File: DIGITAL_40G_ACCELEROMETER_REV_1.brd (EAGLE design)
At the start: 19 x 40.1 mm, 18 parts, among them IC1 ADIS16500AMLZ, IC2 LTC6820IUD#PBF, IC3 LDL1117S33R, T1 782482_33VC

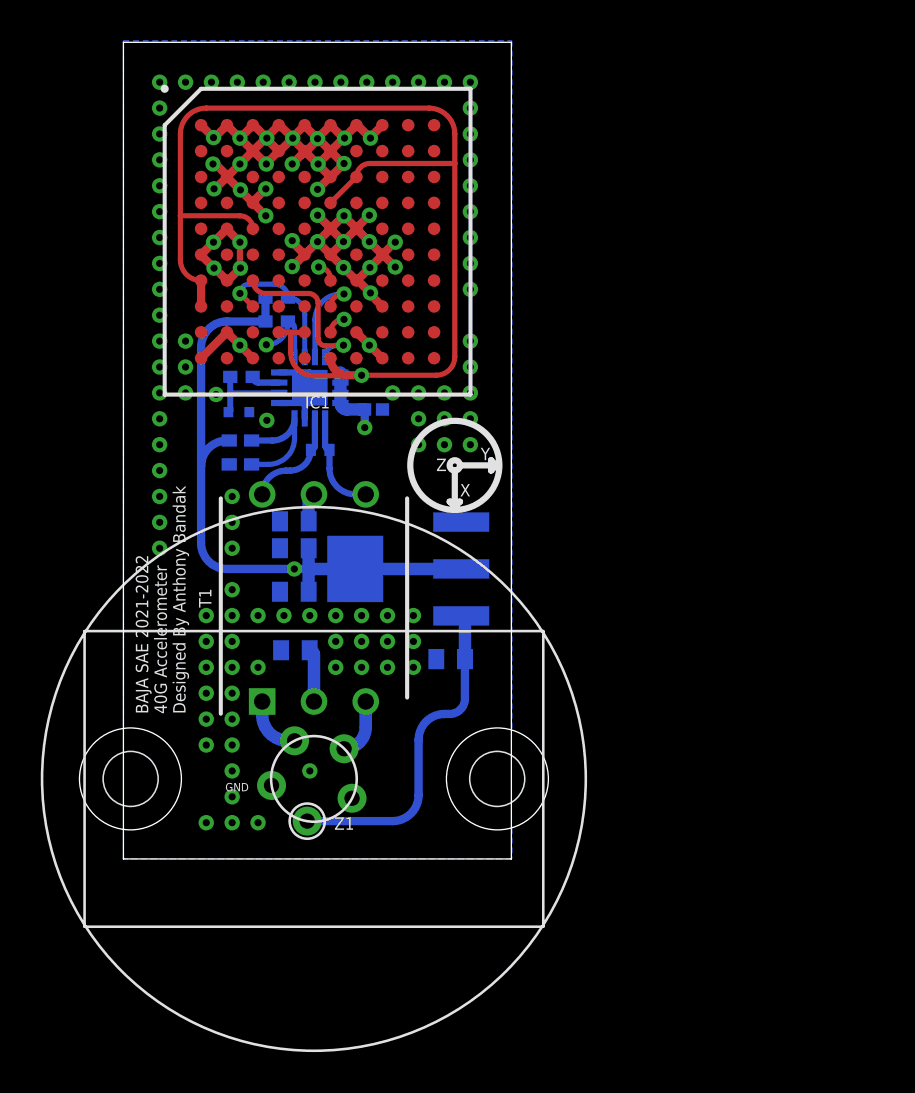
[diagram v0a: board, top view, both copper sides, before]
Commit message: Final Board Layout Update. Incorporated new connector model.
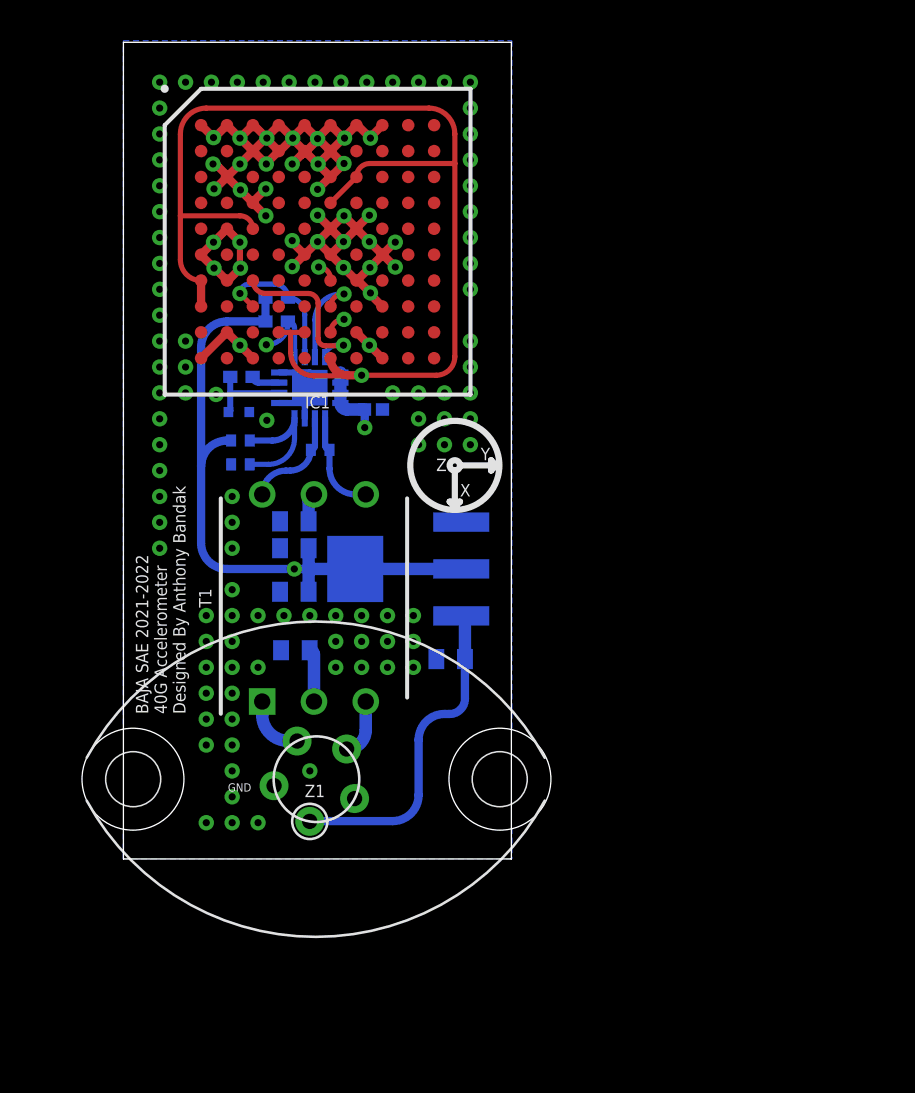
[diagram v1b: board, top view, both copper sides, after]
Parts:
- R11: device TNPW0402100RBYEP:RESC1005X40N -> SamacSys_Parts:RESC1005X40N
- R16, R17: device CRG0402ZR:RESC1005X40N -> SamacSys_Parts:RESC1005X40N
- moved Z1 13.3 mm to (9.40, 3.96)
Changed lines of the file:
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@@
 <drawing>
 <settings>
-<setting alwaysvectorfont="yes"/>
+<setting alwaysvectorfont="no"/>
 <setting verticaltext="up"/>
 </settings>
@@
 </layers>
 <board>
-<fusionsync huburn="a.YnVzaW5lc3M6bXljcHA1NTk" projecturn="a.YnVzaW5lc3M6bXljcHA1NTkjRDIwMjEwOTE1NDQ0OTgwODU2" f3durn="urn:adsk.wipprod:dm.lineage:BeAIdd1JT46-xdl6n52ekA" pcbguid="" lastpulledtime="" lastsyncedchangeguid="" latestrevisionid="1bc7ff69-2360-4ecd-9c21-a148a7abfcbe" lastsyncedrevisionid="1bc7ff69-2360-4ecd-9c21-a148a7abfcbe" lastboardhashguid="e5a5a45a-0394-a7ea-7430-f946065ce0ce" lastpushedtime="2022-03-26T00:00:16Z" linktopcb3d="true"/>
+<fusionsync huburn="a.YnVzaW5lc3M6bXljcHA1NTk" projecturn="a.YnVzaW5lc3M6bXljcHA1NTkjRDIwMjEwOTE1NDQ0OTgwODU2" f3durn="urn:adsk.wipprod:dm.lineage:BeAIdd1JT46-xdl6n52ekA" pcbguid="" lastpulledtime="" lastsyncedchangeguid="" latestrevisionid="42d7c380-4da1-460d-9f28-112faf3eeb5c" lastsyncedrevisionid="42d7c380-4da1-460d-9f28-112faf3eeb5c" lastboardhashguid="adb813b8-7e80-92ce-5e99-bf921410aa5f" lastpushedtime="2022-04-08T20:49:55Z" linktopcb3d="true"/>
 <plain>
 <wire x1="0" y1="0" x2="19.03" y2="0" width="0" layer="20"/>
@@
 <attribute name="NAME" x="13.97" y="18.288" size="0.6096" layer="26" rot="MR0" align="center"/>
 </element>
-<element name="R11" library="TNPW0402100RBYEP" package="RESC1005X40N" value="100" x="9.652" y="20.066" smashed="yes" rot="MR0">
+<element name="R11" library="SamacSys_Parts" library_urn="urn:adsk.eagle:library:34029941" package="RESC1005X40N" package3d_urn="urn:adsk.eagle:package:34740186/6" value="100" x="9.652" y="20.066" smashed="yes" rot="MR0">
 <attribute name="AVAILABILITY" value="In Stock" x="-22.098" y="-28.194" size="1.778" layer="28" rot="MR0" display="off"/>
 <attribute name="DESCRIPTION" value=" 100 Ohms ±0.1% 0.063W, 1/16W Chip Resistor 0402 (1005 Metric) Anti-Sulfur, Automotive AEC-Q200, Moisture Resistant Thin Film " x="-22.098" y="-28.194" size="1.778" layer="28" rot="MR0" display="off"/>
@@
 <attribute name="NAME" x="4.0132" y="12.8016" size="0.6096" layer="25" rot="R90" align="center"/>
 </element>
-<element name="Z1" library="SamacSys_Parts" library_urn="urn:adsk.eagle:library:31941355" package="AS_FEMALE_5_PIN" package3d_urn="urn:adsk.eagle:package:34263750/6" value="AS_FEMALE_5_PIN" x="20.574" y="11.176" smashed="yes" rot="R180">
-<attribute name="NAME" x="10.8372" y="1.7346" size="0.6096" layer="25" rot="R180" align="center"/>
-</element>
-<element name="R16" library="CRG0402ZR" package="RESC1005X40N" value="CRG0402ZR" x="5.7404" y="19.3548" smashed="yes" rot="MR0">
+<element name="Z1" library="SamacSys_Parts" library_urn="urn:adsk.eagle:library:31941355" package="AS_FEMALE_5_PIN" package3d_urn="urn:adsk.eagle:package:34263750/8" value="AS_FEMALE_5_PIN" x="9.398" y="3.9624" smashed="yes" rot="R180">
+<attribute name="NAME" x="9.3894" y="3.3348" size="0.6096" layer="25" rot="R180" align="center"/>
+</element>
+<element name="R16" library="SamacSys_Parts" library_urn="urn:adsk.eagle:library:34029941" package="RESC1005X40N" package3d_urn="urn:adsk.eagle:package:34740186/6" value="CRG0402ZR" x="5.7404" y="19.3548" smashed="yes" rot="MR0">
 <attribute name="DESCRIPTION" value="0 0402 Thick Film Surface Mount Fixed Resistor +/-0% 0.063W CRG0402ZR" x="5.7404" y="19.3548" size="1.778" layer="28" rot="MR0" display="off"/>
 <attribute name="HEIGHT" value="0.4mm" x="5.7404" y="19.3548" size="1.778" layer="28" rot="MR0" display="off"/>
@@
 <attribute name="NAME" x="3.5814" y="19.3548" size="0.6096" layer="26" rot="MR0" align="center"/>
 </element>
-<element name="R17" library="CRG0402ZR" package="RESC1005X40N" value="CRG0402ZR" x="5.7404" y="20.5232" smashed="yes" rot="MR0">
+<element name="R17" library="SamacSys_Parts" library_urn="urn:adsk.eagle:library:34029941" package="RESC1005X40N" package3d_urn="urn:adsk.eagle:package:34740186/6" value="CRG0402ZR" x="5.7404" y="20.5232" smashed="yes" rot="MR0">
 <attribute name="DESCRIPTION" value="0 0402 Thick Film Surface Mount Fixed Resistor +/-0% 0.063W CRG0402ZR" x="5.7404" y="20.5232" size="1.778" layer="28" rot="MR0" display="off"/>
 <attribute name="HEIGHT" value="0.4mm" x="5.7404" y="20.5232" size="1.778" layer="28" rot="MR0" display="off"/>
@@
 <wire x1="10.16" y1="25.8318" x2="10.795" y2="26.4668" width="0.254" layer="1" curve="-90"/>
 <wire x1="10.795" y1="26.4668" x2="10.8204" y2="26.4668" width="0.254" layer="1"/>
-<wire x1="11.215" y1="2.976" x2="12.446" y2="2.976" width="0.254" layer="2"/>
-<wire x1="12.446" y1="2.976" x2="13.716" y2="4.246" width="0.254" layer="2" curve="90"/>
+<wire x1="13.716" y1="4.246" x2="12.446" y2="2.976" width="0.254" layer="2" curve="-90"/>
 <wire x1="13.716" y1="6.604" x2="14.986" y2="7.874" width="0.254" layer="2" curve="-90"/>
 <wire x1="17.78" y1="9.144" x2="16.51" y2="7.874" width="0.254" layer="2" curve="-90"/>
@@
 <wire x1="16.51" y1="26.4668" x2="17.78" y2="25.1968" width="0.254" layer="2" curve="-90"/>
 <wire x1="17.78" y1="25.1968" x2="17.78" y2="9.144" width="0.254" layer="2"/>
+<wire x1="12.446" y1="2.976" x2="11.3526" y2="2.976" width="0.254" layer="2"/>
+<wire x1="11.3526" y1="2.976" x2="11.339" y2="2.9624" width="0.254" layer="2" curve="90"/>
 </signal>
 <signal name="IP">
 <contactref element="T1" pad="1"/>
 <contactref element="Z1" pad="5"/>
-<wire x1="8.395" y1="5.796" x2="8.0772" y2="5.796" width="0.6096" layer="16"/>
 <wire x1="8.0772" y1="5.796" x2="6.8072" y2="7.066" width="0.6096" layer="16" curve="-90"/>
 <wire x1="6.8072" y1="7.066" x2="6.8072" y2="7.7216" width="0.6096" layer="16"/>
+<wire x1="8.519" y1="5.7824" x2="8.0908" y2="5.7824" width="0.6096" layer="16"/>
+<wire x1="8.0908" y1="5.7824" x2="8.0772" y2="5.796" width="0.6096" layer="16" curve="-90"/>
 </signal>
 <signal name="IM">
 <contactref element="T1" pad="3"/>
 <contactref element="Z1" pad="4"/>
-<wire x1="10.825" y1="5.406" x2="11.8872" y2="6.4682" width="0.6096" layer="16" curve="90"/>
-<wire x1="11.8872" y1="6.4682" x2="11.8872" y2="7.7216" width="0.6096" layer="16"/>
+<wire x1="11.8872" y1="6.3306" x2="10.949" y2="5.3924" width="0.6096" layer="16" curve="-90"/>
+<wire x1="11.8872" y1="7.7216" x2="11.8872" y2="6.3306" width="0.6096" layer="16"/>
 </signal>
 <signal name="12V">
@@
 <wire x1="16.7528" y1="9.8044" x2="16.7528" y2="11.7412" width="0.6096" layer="16"/>
 <wire x1="16.7528" y1="11.7412" x2="16.57" y2="11.924" width="0.6096" layer="16" curve="90"/>
-<wire x1="9.015" y1="1.856" x2="13.208" y2="1.856" width="0.4064" layer="16"/>
-<wire x1="13.208" y1="1.856" x2="14.478" y2="3.126" width="0.4064" layer="16" curve="90"/>
+<wire x1="14.478" y1="3.126" x2="13.208" y2="1.856" width="0.4064" layer="16" curve="-90"/>
 <wire x1="14.478" y1="5.842" x2="15.748" y2="7.112" width="0.4064" layer="16" curve="-90"/>
 <wire x1="15.748" y1="7.112" x2="16.002" y2="7.112" width="0.4064" layer="16"/>
@@
 <wire x1="16.7528" y1="7.8628" x2="16.7528" y2="9.8044" width="0.4064" layer="16"/>
 <wire x1="14.478" y1="3.126" x2="14.478" y2="5.842" width="0.4064" layer="16"/>
+<wire x1="13.208" y1="1.856" x2="9.1526" y2="1.856" width="0.4064" layer="16"/>
+<wire x1="9.1526" y1="1.856" x2="9.139" y2="1.8424" width="0.4064" layer="16" curve="90"/>
 </signal>
 <signal name="3.3V">
@@
 <wire x1="11.8364" y1="22.039" x2="11.8282" y2="22.0472" width="0.4064" layer="16" curve="90"/>
 <wire x1="12.954" y1="15.494" x2="12.954" y2="20.0406" width="0.4064" layer="2"/>
-<wire x1="5.1904" y1="20.5232" x2="5.08" y2="20.5232" width="0.4064" layer="16"/>
+<wire x1="5.2834" y1="20.5232" x2="5.08" y2="20.5232" width="0.4064" layer="16"/>
 <wire x1="5.08" y1="20.5232" x2="3.81" y2="19.2532" width="0.4064" layer="16" curve="90"/>
 <wire x1="3.81" y1="15.494" x2="5.08" y2="14.224" width="0.4064" layer="16" curve="90"/>
@@
 <contactref element="R17" pad="1"/>
 <wire x1="8.394" y1="21.614" x2="7.3032" y2="20.5232" width="0.3048" layer="16" curve="-90"/>
-<wire x1="7.3032" y1="20.5232" x2="6.2904" y2="20.5232" width="0.3048" layer="16"/>
+<wire x1="7.3032" y1="20.5232" x2="6.1974" y2="20.5232" width="0.3048" layer="16"/>
 <wire x1="8.394" y1="21.614" x2="8.394" y2="20.6248" width="0.254" layer="16"/>
 <wire x1="8.394" y1="20.6248" x2="7.124" y2="19.3548" width="0.254" layer="16" curve="-90"/>
-<wire x1="7.124" y1="19.3548" x2="6.2904" y2="19.3548" width="0.254" layer="16"/>
+<wire x1="7.124" y1="19.3548" x2="6.1974" y2="19.3548" width="0.254" layer="16"/>
 </signal>
 <signal name="N$1">

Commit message: Final final board layout update. Screw mounted now.
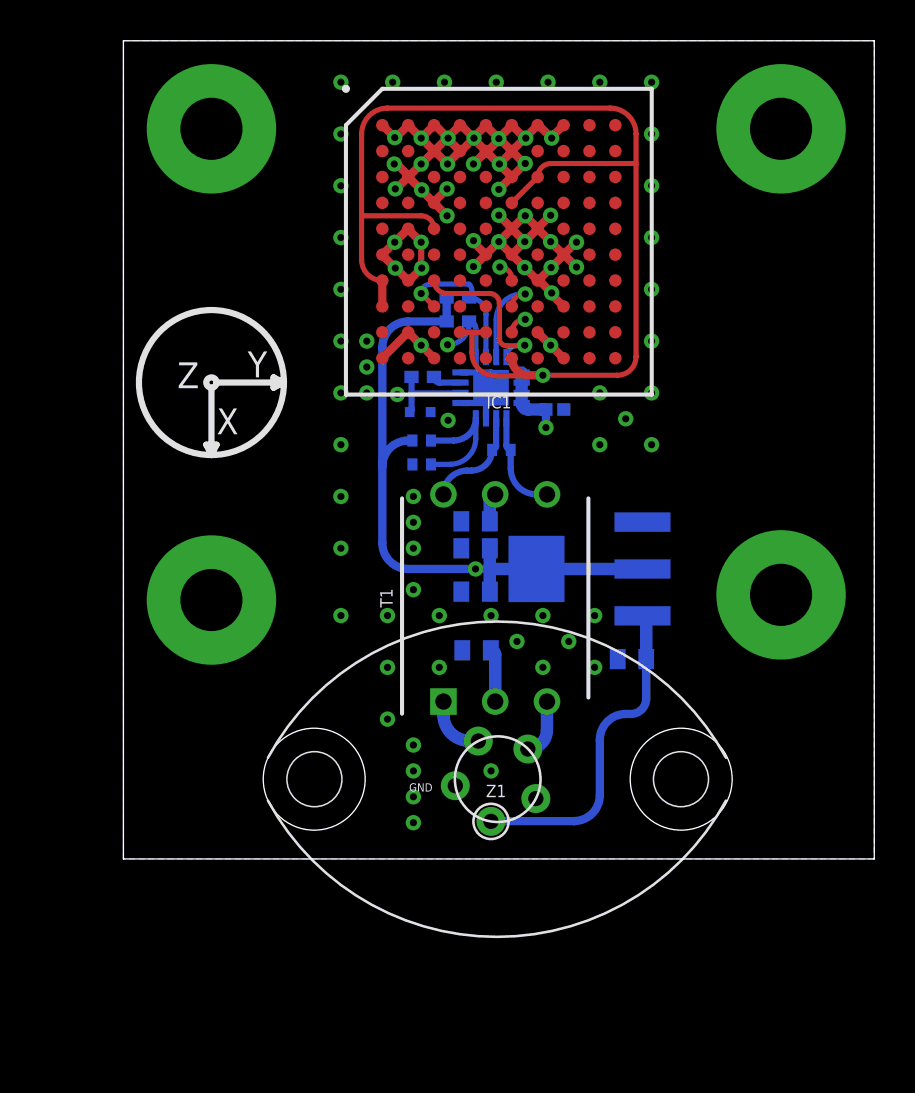
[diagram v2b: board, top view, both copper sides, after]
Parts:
- added U$1, U$2, U$3, U$4: THROUGH_HOLE, SamacSys_Parts:1/16TH_BOLT
- moved R11 8.89 mm to (18.5, 20.1)
- moved C4 8.89 mm to (21.2, 22.0)
- moved C5 8.89 mm to (17.3, 10.2)
- moved R12 8.89 mm to (16.4, 26.4)
- moved R13 8.89 mm to (16.4, 27.5)
- moved R14 8.89 mm to (14.7, 23.6)
- moved R15 8.89 mm to (14.6, 21.9)
- moved R16 8.89 mm to (14.6, 19.4)
- moved R17 8.89 mm to (14.6, 20.5)
- moved T1 8.89 mm to (18.2, 12.8)
- moved Z1 8.89 mm to (18.3, 3.96)
- moved C2 8.89 mm to (17.3, 15.2)
- moved C3 8.89 mm to (17.3, 13.1)
- moved C6 8.89 mm to (17.3, 16.6)
- moved IC1 8.89 mm to (18.4, 30.3)
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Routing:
- net GND: vias 131 -> 90
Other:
- board size 19 x 40.1 mm -> 36.8 x 40.1 mm

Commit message: Final final preliminary board layout update. Back to 2 screw holes and sized at 1.25 inches square.
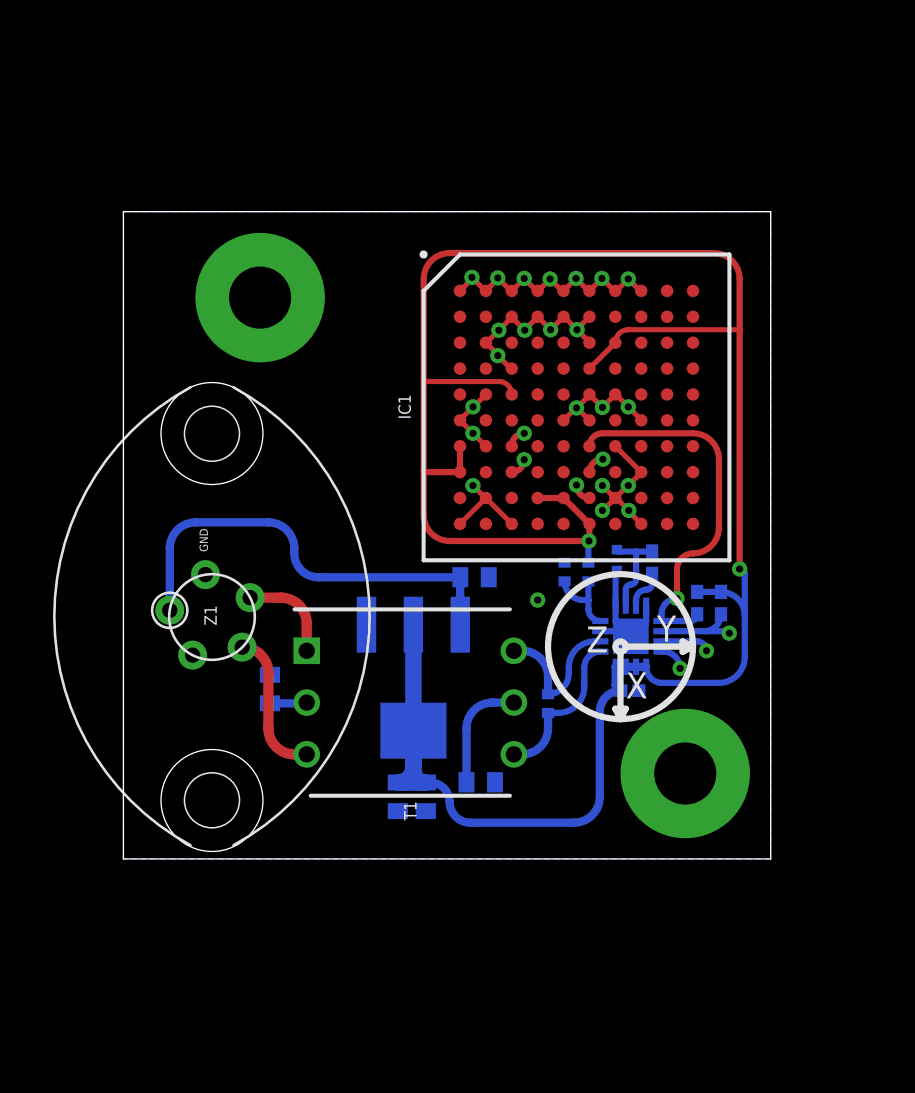
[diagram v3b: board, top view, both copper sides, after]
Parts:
- removed U$1, U$2: THROUGH_HOLE, SamacSys_Parts:1/16TH_BOLT
- moved U$3 26.9 mm to (6.71, 27.5), flipped to the bottom, turned to 180 degrees
- moved R13 19.8 mm to (29.3, 12.5), turned to 90 degrees
- moved R12 18.1 mm to (28.1, 12.5), turned to 90 degrees
- moved Z1 16.0 mm to (4.39, 11.9), turned to 90 degrees
- moved R14 14.5 mm to (25.9, 14.5), turned to 90 degrees
- moved C4 14.3 mm to (24.8, 8.26)
- moved IC2 14.0 mm to (24.9, 10.9), turned to 0 degrees
- moved C6 12.8 mm to (17.5, 3.76), turned to 180 degrees
- moved C2 12.8 mm to (13.5, 3.05), turned to 270 degrees
- moved R11 12.7 mm to (20.8, 7.62), turned to 90 degrees
- moved R15 12.1 mm to (24.2, 14.7), turned to 90 degrees
- moved R17 10.4 mm to (22.8, 14.1), turned to 90 degrees
- moved C3 10.3 mm to (14.8, 3.05), turned to 270 degrees
- moved C5 10.3 mm to (7.19, 8.33), turned to 90 degrees
- moved IC3 10.2 mm to (14.2, 8.89), turned to 270 degrees
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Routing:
- net GND: track 73.4 -> 50.9 mm, vias 90 -> 22
- net MISO: track 7.36 -> 21.8 mm, vias 1 -> 2
- net CS: track 7.94 -> 20.7 mm, vias 1 -> 3
- net SCK: track 4.69 -> 16.3 mm, vias 1 -> 2
- net DR: track 34.8 -> 25.4 mm
- net MOSI: track 10.0 -> 18.1 mm, vias 2 -> 1
- net 3.3V: track 108.4 -> 115.2 mm, vias 3 -> 2
- net 12V: track 15.8 -> 21.4 mm
- net IM: track 2.72 -> 6.94 mm
- net N$1: track 1.43 -> 5.49 mm
- net SLOW: track 6.36 -> 3.73 mm
- net IMBOARD: track 4.86 -> 7.33 mm
- net IPBOARD: track 4.92 -> 6.89 mm
- net IP: track 2.90 -> 4.64 mm
- net N$2: track 2.60 -> 1.82 mm
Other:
- board size 36.8 x 40.1 mm -> 31.8 x 31.8 mm

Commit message: Added a couple of ground stitching vias
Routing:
- net GND: vias 22 -> 27
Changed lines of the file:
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@@
 <drawing>
 <settings>
-<setting alwaysvectorfont="yes"/>
+<setting alwaysvectorfont="no"/>
 <setting verticaltext="up"/>
 </settings>
@@
 <wire x1="22.86" y1="25.3238" x2="22.842040625" y2="25.367159375" width="0.254" layer="1" curve="45"/>
 <wire x1="22.842040625" y1="25.367159375" x2="22.2504" y2="25.9588" width="0.254" layer="1"/>
+<via x="3.302" y="15.24" extent="1-16" drill="0.35"/>
+<via x="4.572" y="15.24" extent="1-16" drill="0.35"/>
+<via x="6.096" y="15.24" extent="1-16" drill="0.35"/>
+<via x="7.366" y="15.24" extent="1-16" drill="0.35"/>
+<via x="7.366" y="13.97" extent="1-16" drill="0.35"/>
 </signal>
 <signal name="DR">
